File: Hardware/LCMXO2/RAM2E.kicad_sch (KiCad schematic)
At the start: 66 parts, among them J1 AppleIIeAux, J2 JTAG, J3 C14M, U1 LCMXO2-TG100, U2 W9812G6KH-6, U3 74LVC245APW, U4 74LVC245APW, U5 74LVC245APW, U6 74AHCT245PW, U7 74AHCT245PW, U8 XC6206P332MR, U9 AP2127K-1.2TRG1

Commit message: Change BOM to separate U4 from U3 and U5
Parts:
- U3, U5: value 74LVC245APW -> 74AHC245PW; LCSC Part C6082 -> C5516
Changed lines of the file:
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@@
       (effects (font (size 1.27 1.27)))
     )
-    (property "Value" "74LVC245APW" (at 76.2 53.34 0)
+    (property "Value" "74AHC245PW" (at 76.2 53.34 0)
       (effects (font (size 1.27 1.27)))
     )
@@
       (effects (font (size 1.524 1.524)) hide)
     )
-    (property "LCSC Part" "C6082" (at 76.2 38.1 0)
+    (property "LCSC Part" "C5516" (at 76.2 38.1 0)
       (effects (font (size 1.27 1.27)) hide)
     )
@@
       (effects (font (size 1.27 1.27)))
     )
-    (property "Value" "74LVC245APW" (at 76.2 119.38 0)
+    (property "Value" "74AHC245PW" (at 76.2 119.38 0)
       (effects (font (size 1.27 1.27)))
     )
@@
       (effects (font (size 1.524 1.524)) hide)
     )
-    (property "LCSC Part" "C6082" (at 76.2 104.14 0)
+    (property "LCSC Part" "C5516" (at 76.2 104.14 0)
       (effects (font (size 1.27 1.27)) hide)
     )

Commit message: RC 2.1
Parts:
- removed D1: Amber, stdpads:LED_0805, symbol Device:D_Small_ALT
- removed J2: JTAG, stdpads:TC2050, symbol Connector_Generic:Conn_02x05_Odd_Even
- removed J3: C14M, Connector_PinHeader_2.54mm:PinHeader_1x02_P2.54mm_Vertical, symbol Connector_Generic:Conn_01x02
- removed U9: AP2127K-1.2TRG1, stdpads:SOT-23-5, symbol Regulator_Linear:AP2127K-1.2
- added C32, C33: 22p, stdpads:C_0603, symbol Device:C_Small
- added C34, C36, C37: 2u2, stdpads:C_0603, symbol Device:C_Small
- added D1: Amber, stdpads:LED_0805, symbol Device:LED_Small_ALT
- added J2: microUSB, stdpads:USB_Micro-B_Amphenol_10118192-0001, symbol Connector:USB_B_Micro
- added J3: C14M, stdpads:EdgeClipHole, symbol Connector_Generic:Conn_01x01
- added J4: C14M, stdpads:PinHeader_1x02_P2.54mm_Vertical, symbol Connector_Generic:Conn_01x02
- added J5: JTAG, stdpads:Tag-Connect_TC2050-IDC-FP_2x05_P1.27mm_Vertical, symbol Connector_Generic:Conn_02x05_Odd_Even
- added R22: 47, stdpads:R_0603, symbol Device:R_Small
- added U10: CH340G, stdpads:SOIC-16_3.9mm, symbol Interface_USB:CH340G
- added U11: 74AHCT1G125GW, stdpads:SOT-353, symbol GW_Logic:741G125GW
- added U9: AP2127K-1.2TRG1, stdpads:SOT-23-5, symbol Regulator_Linear:AP2127K-1.8
- added Y1: 12M, stdpads:Crystal_SMD_3225-4Pin_3.2x2.5mm, symbol Device:Crystal_GND24_Small
- C1, C2, C3, C4, C5, C6: Mfg. Part Numbers Samsung CL21A106KAYNNNE -> (none); Notes 10V or higher. Any manufacturer's part is acceptable but Sa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 -> (none)
- C10, C11, C12, C13, C14, C15, C16, C17, C18, C19, C20, C21, C22, C23, C24, C25, C26, C27, C28, C30, C7, C8, C9: Mfg. Part Numbers Samsung CL10A225KO8NNNC -> (none); Notes 10V or higher. Any manufacturer's part is acceptable but Sa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 -> (none)
- C29: value 10u -> 2u2; footprint stdpads:C_0805 -> stdpads:C_0603; LCSC Part C15850 -> C23630; Mfg. Part Numbers Samsung CL21A106KAYNNNE -> (none); Notes 10V or higher. Any manufacturer's part is acceptable but Sa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 -> (none)
- C31: value 15p -> 22p; LCSC Part C1644 -> C1653; Mfg. Part Numbers Samsung CL10C150JB8NNNC -> (none); Notes 10V or higher. Any manufacturer's part is acceptable but Sa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 -> (none)
- FID1, FID2, FID3, FID4: Notes DNP - SMT vision system fiducial -> (none)
- H1, H2, H3, H4: Notes DNP - mounting hole for solder paste printing -> (none)
- H5: Notes DNP - mounting hole -> (none)
- J1: Notes DNP - edge connector -> (none)
- R1: Mfg. Part Numbers Uniroyal 0805W8F0000T5E -> (none); Notes Any manufacturer's part is acceptable. -> (none)
- R10: Mfg. Part Numbers Uniroyal 0805W8F2200T5E -> (none); Notes Any manufacturer's part is acceptable. -> (none)
- R11: Mfg. Part Numbers Uniroyal 0603WAF1002T5E -> (none); Notes Any manufacturer's part is acceptable. -> (none)
- R12, R13, R2, R3: Mfg. Part Numbers Uniroyal 0603WAF470JT5E -> (none); Notes Any manufacturer's part is acceptable. -> (none)
- R4: value 47 -> DNP; LCSC Part C23182 -> (none); Mfg. Part Numbers Uniroyal 0603WAF470JT5E -> (none); Notes Any manufacturer's part is acceptable. -> (none)
- R5, R8, R9: value 10k -> DNP; LCSC Part C25804 -> (none); Mfg. Part Numbers Uniroyal 0603WAF1002T5E -> (none); Notes Any manufacturer's part is acceptable. -> (none)
- R6: value 0 -> 2k2; footprint stdpads:R_0805 -> stdpads:R_0603; LCSC Part C17477 -> C4190; Mfg. Part Numbers Uniroyal 0805W8F0000T5E -> (none); Notes Any manufacturer's part is acceptable. -> (none)
- R7: footprint stdpads:R_0805 -> stdpads:R_0603
- U1: value LCMXO2-TG100 -> LCMXO2-640HC-4TG100C; Mfg. Part Numbers Lattice LCMXO2-640HC-4TG100C, Lattice LCMXO2-640HC-5TG100C,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 -> (none)
- U2: Mfg. Part Numbers Winbond W9812G6KH-6, Winbond W9812G6KH-6I, Winbond W9825G6K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 -> (none); Notes Most 166 MHz 128/256 Mbit x16 SDRAM is acceptable. -> (none)
- U3, U4, U5: Mfg. Part Numbers NXP 74LVC245APW, TI SN74LVC245APW, NXP 74AHC245PW, NXP 74AH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 -> (none); Notes Most 74LVC245 or 74AHC245 in TSSOP-20 package is acceptable. -> (none)
- U6, U7: Mfg. Part Numbers NXP 74AHCT245PW, NXP 74AHCT245APW, TI SN74AHCT245PW -> (none); Notes Most 74AHCT245 in TSSOP-20 package is acceptable. -> (none)
- U8: Mfg. Part Numbers Torex XC6206P332MR -> (none); Notes Most 3.3V regulator in SOT-23 package is acceptable. -> (none)
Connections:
- net +1V2: now also U9.5 (VOUT)
- net +3V3: now also R6.1, R9.1, C34.1, C36.1, J5.6 (Pin_6), U10.10 (~{DSR}), U10.11 (~{RI}), U10.16 (VCC), U10.3 (RXD), U10.4 (V3); no longer C30.1
- net +5V: now also C30.1, U11.5 (Vcc), U9.1 (VIN), U9.3 (EN)
- net ACLK: now also R12.1; no longer R13.1
- net AN3: now also U11.2 (A); no longer R6.2, R7.2
- net C14MB: now also R13.1, J3.1 (Pin_1), J4.1 (Pin_1); no longer R3.1
- net GND: now also R7.2, C32.2, C33.2, C34.2, C36.2, C37.2, J2.5 (GND), J2.6 (Shield), J4.2 (Pin_2), J5.2 (Pin_2), J5.4 (Pin_4), U10.1 (GND), U10.12 (~{DCD}), U10.15 (R232), U11.3 (GND), U9.2 (GND), Y1.2, Y1.4; no longer R9.2
- net LED: now also D1.1 (K)
- net RCLK: now also R3.1; no longer R12.1
- net R~{W}: now also U3.3 (A1); no longer U3.2 (A0)
- net R~{W}in: now also U3.17 (B1); no longer U3.18 (B0)
- net TCK: now also C31.1, R4.1, R7.1, U1.91 (TCK/PT7C), R22.2; no longer R4.2
- net TCKr: now also R4.2, J5.1 (Pin_1); no longer C31.1, R4.1, R9.1, U1.91 (TCK/PT7C)
- net TDI: now also J5.5 (Pin_5), U10.13 (~{DTR})
- net TDO: now also J5.7 (Pin_7), U10.9 (~{CTS})
- net TMS: now also R9.2, J5.3 (Pin_3), U10.14 (~{RTS})
- net ~{C07X}: now also U3.2 (A0); no longer U3.3 (A1)
- net ~{C07X}in: now also U3.18 (B0); no longer U3.17 (B1)
- net ~{FRCTXT}: now also U11.4 (Y); no longer R6.1, R7.1
- net at R12.2, U4.16 (B2): now also R3.2; no longer R13.2
- net at U4.18 (B0): now also R13.2; no longer R3.2
- net DHGR~{OE}: now reaches U1.47 (PB14)
- net DHGR~{OE}: now also R6.2, U11.1 (~{OE})
- net at R10.1: now also D1.2 (A)
- new net: C33.1, U10.7 (XI), Y1.1
- new net: C32.1, U10.8 (XO), Y1.3
- new net: J2.2 (D-), U10.6 (UD-)
- new net: J2.3 (D+), U10.5 (UD+)
- new net USB5V: C37.1, J2.1 (VBUS)
- new net UTCK: R22.1, U10.2 (TXD)
- no-connect marks 4 -> 5
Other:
- moved on the sheet: R11, R5, R8

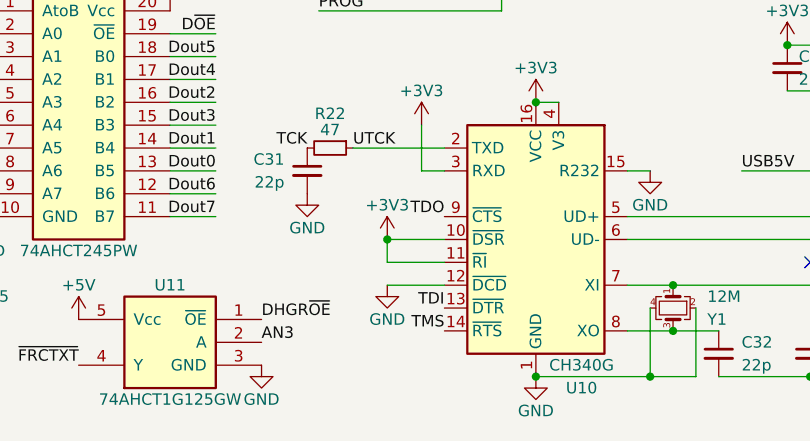
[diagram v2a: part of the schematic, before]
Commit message: RC
Fix board IDs
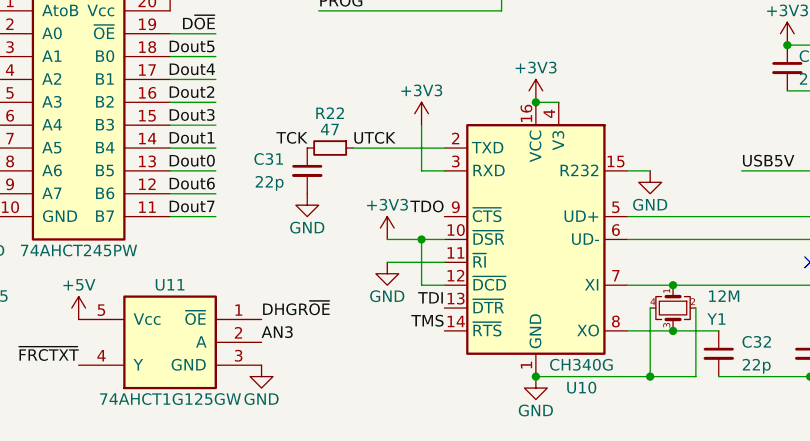
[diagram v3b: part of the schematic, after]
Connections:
- net +3V3: now also U10.12 (~{DCD}); no longer U10.11 (~{RI})
- net GND: now also U10.11 (~{RI}); no longer U10.12 (~{DCD})
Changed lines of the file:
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@@
   (junction (at 168.91 165.1) (diameter 0) (color 0 0 0 0)
   )
+  (junction (at 99.06 181.61) (diameter 0) (color 0 0 0 0)
+  )
   (junction (at 208.28 80.01) (diameter 0) (color 0 0 0 0)
   )
@@
   )
   (junction (at 199.39 19.05) (diameter 0) (color 0 0 0 0)
-  )
-  (junction (at 95.25 181.61) (diameter 0) (color 0 0 0 0)
   )
   (junction (at 198.12 85.09) (diameter 0) (color 0 0 0 0)
@@
     (stroke (width 0) (type default))
   )
-  (wire (pts (xy 95.25 186.69) (xy 101.6 186.69))
-    (stroke (width 0) (type default))
-  )
   (wire (pts (xy 38.1 83.82) (xy 34.29 83.82))
     (stroke (width 0) (type default))
   )
+  (wire (pts (xy 101.6 186.69) (xy 99.06 186.69))
+    (stroke (width 0) (type default))
+  )
   (wire (pts (xy 129.54 196.85) (xy 124.46 196.85))
     (stroke (width 0) (type default))
@@
     (stroke (width 0) (type default))
   )
+  (wire (pts (xy 99.06 186.69) (xy 99.06 181.61))
+    (stroke (width 0) (type default))
+  )
   (wire (pts (xy 45.72 102.87) (xy 50.8 102.87))
     (stroke (width 0) (type default))
@@
     (stroke (width 0) (type default))
   )
+  (wire (pts (xy 99.06 181.61) (xy 101.6 181.61))
+    (stroke (width 0) (type default))
+  )
   (wire (pts (xy 114.3 44.45) (xy 119.38 44.45))
     (stroke (width 0) (type default))
@@
     (stroke (width 0) (type default))
   )
-  (wire (pts (xy 95.25 181.61) (xy 101.6 181.61))
+  (wire (pts (xy 95.25 181.61) (xy 99.06 181.61))
     (stroke (width 0) (type default))
   )
@@
   )
   (wire (pts (xy 199.39 19.05) (xy 199.39 21.59))
-    (stroke (width 0) (type default))
-  )
-  (wire (pts (xy 95.25 184.15) (xy 95.25 181.61))
     (stroke (width 0) (type default))
   )
@@
     )
   )
-  (symbol (lib_id "power:GND") (at 95.25 186.69 0) (mirror y) (unit 1)
+  (symbol (lib_id "power:GND") (at 95.25 184.15 0) (mirror y) (unit 1)
     (in_bom yes) (on_board yes) (dnp no)
-    (property "Reference" "#PWR033" (at 95.25 193.04 0)
-      (effects (font (size 1.27 1.27)) hide)
-    )
-    (property "Value" "GND" (at 95.25 190.5 0)
+    (property "Reference" "#PWR033" (at 95.25 190.5 0)
+      (effects (font (size 1.27 1.27)) hide)
+    )
+    (property "Value" "GND" (at 95.25 187.96 0)
       (effects (font (size 1.27 1.27)))
     )
-    (property "Footprint" "" (at 95.25 186.69 0)
-      (effects (font (size 1.27 1.27)) hide)
-    )
-    (property "Datasheet" "" (at 95.25 186.69 0)
-      (effects (font (size 1.27 1.27)) hide)
-    )
+    (property "Footprint" "" (at 95.25 184.15 0)
+      (effects (font (size 1.27 1.27)) hide)
+    )
+    (property "Datasheet" "" (at 95.25 184.15 0)
+      (effects (font (size 1.27 1.27)) hide)
+    )

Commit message: RC
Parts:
- added R14, R15: 2k2, stdpads:R_0603, symbol Device:R_Small
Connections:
- net +3V3: now also R14.1, R15.1
- net D~{OE}: now also R15.2
- net V~{OE}: now also R14.2
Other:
- moved on the sheet: R11, R5, R8

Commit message: RC
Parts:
- U3, U5: value 74AHC245PW -> 74LVC245APW; LCSC Part C5516 -> C6082
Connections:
- no-connect marks 5 -> 6
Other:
- title: GW4203B (RAM2E II) - LCMXO2-640 / LCMXO2-1200 -> GW4203C (RAM2E II) - LCMXO2-640 / LCMXO2-1200
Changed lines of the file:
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@@
   (paper "USLetter")
   (title_block
-    (title "GW4203B (RAM2E II) - LCMXO2-640 / LCMXO2-1200")
-    (date "2024-04-24")
-    (rev "2.1")
+    (title "GW4203C (RAM2E II) - LCMXO2-640 / LCMXO2-1200")
+    (date "2024-05-20")
+    (rev "1.0")
     (company "Garrett's Workshop")
   )
@@
   (no_connect (at 71.12 64.77))
   (no_connect (at 142.24 184.15))
+  (no_connect (at 119.38 125.73))
   (no_connect (at 21.59 88.9))
   (bus_entry (at 210.82 107.95) (size -2.54 2.54)
@@
       (effects (font (size 1.27 1.27)))
     )
-    (property "Value" "74AHC245PW" (at 60.96 50.8 0)
+    (property "Value" "74LVC245APW" (at 60.96 50.8 0)
       (effects (font (size 1.27 1.27)))
     )
@@
       (effects (font (size 1.524 1.524)) hide)
     )
-    (property "LCSC Part" "C5516" (at 60.96 35.56 0)
+    (property "LCSC Part" "C6082" (at 60.96 35.56 0)
       (effects (font (size 1.27 1.27)) hide)
     )
@@
       (effects (font (size 1.27 1.27)))
     )
-    (property "Value" "74AHC245PW" (at 60.96 116.84 0)
+    (property "Value" "74LVC245APW" (at 60.96 116.84 0)
       (effects (font (size 1.27 1.27)))
     )
@@
       (effects (font (size 1.524 1.524)) hide)
     )
-    (property "LCSC Part" "C5516" (at 60.96 101.6 0)
+    (property "LCSC Part" "C6082" (at 60.96 101.6 0)
       (effects (font (size 1.27 1.27)) hide)
     )

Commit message: RC
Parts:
- C29: value 2u2 -> 10u; footprint stdpads:C_0603 -> stdpads:C_0805; LCSC Part C23630 -> C15850
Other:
- moved on the sheet: C30
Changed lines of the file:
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@@
   (junction (at 218.44 54.61) (diameter 0) (color 0 0 0 0)
   )
+  (junction (at 208.28 85.09) (diameter 0) (color 0 0 0 0)
+  )
   (junction (at 218.44 69.85) (diameter 0) (color 0 0 0 0)
   )
@@
   (junction (at 99.06 181.61) (diameter 0) (color 0 0 0 0)
   )
-  (junction (at 208.28 80.01) (diameter 0) (color 0 0 0 0)
-  )
   (junction (at 228.6 74.93) (diameter 0) (color 0 0 0 0)
   )
@@
   (junction (at 228.6 44.45) (diameter 0) (color 0 0 0 0)
   )
-  (junction (at 218.44 85.09) (diameter 0) (color 0 0 0 0)
-  )
   (junction (at 187.96 19.05) (diameter 0) (color 0 0 0 0)
   )
@@
   (junction (at 187.96 80.01) (diameter 0) (color 0 0 0 0)
   )
+  (junction (at 218.44 85.09) (diameter 0) (color 0 0 0 0)
+  )
   (junction (at 238.76 85.09) (diameter 0) (color 0 0 0 0)
   )
@@
   (junction (at 17.78 36.83) (diameter 0) (color 0 0 0 0)
   )
+  (junction (at 208.28 80.01) (diameter 0) (color 0 0 0 0)
+  )
   (junction (at 238.76 54.61) (diameter 0) (color 0 0 0 0)
   )
@@
   (junction (at 218.44 74.93) (diameter 0) (color 0 0 0 0)
   )
-  (junction (at 208.28 85.09) (diameter 0) (color 0 0 0 0)
-  )
   (junction (at 198.12 74.93) (diameter 0) (color 0 0 0 0)
   )
@@
     (stroke (width 0) (type default))
   )
+  (wire (pts (xy 208.28 85.09) (xy 218.44 85.09))
+    (stroke (width 0) (type default))
+  )
   (wire (pts (xy 114.3 87.63) (xy 119.38 87.63))
     (stroke (width 0) (type default))
@@
     (stroke (width 0) (type default))
   )
-  (wire (pts (xy 218.44 85.09) (xy 228.6 85.09))
-    (stroke (width 0) (type default))
-  )
   (wire (pts (xy 114.3 69.85) (xy 119.38 69.85))
     (stroke (width 0) (type default))
@@
     (stroke (width 0) (type default))
   )
+  (wire (pts (xy 208.28 80.01) (xy 218.44 80.01))
+    (stroke (width 0) (type default))
+  )
   (wire (pts (xy 138.43 21.59) (xy 140.97 21.59))
     (stroke (width 0) (type default))
@@
     (stroke (width 0) (type default))
   )
-  (wire (pts (xy 208.28 85.09) (xy 218.44 85.09))
-    (stroke (width 0) (type default))
-  )
   (wire (pts (xy 45.72 31.75) (xy 50.8 31.75))
     (stroke (width 0) (type default))
@@
     (stroke (width 0) (type default))
   )
+  (wire (pts (xy 218.44 85.09) (xy 228.6 85.09))
+    (stroke (width 0) (type default))
+  )
   (wire (pts (xy 218.44 44.45) (xy 218.44 41.91))
     (stroke (width 0) (type default))
@@
     (stroke (width 0) (type default))
   )
-  (wire (pts (xy 208.28 80.01) (xy 218.44 80.01))
-    (stroke (width 0) (type default))
-  )
   (wire (pts (xy 76.2 161.29) (xy 71.12 161.29))
     (stroke (width 0) (type default))
@@
     )
   )
-  (symbol (lib_id "Device:C_Small") (at 218.44 82.55 0) (unit 1)
+  (symbol (lib_id "Device:C_Small") (at 208.28 82.55 0) (unit 1)
     (in_bom yes) (on_board yes) (dnp no)
-    (property "Reference" "C30" (at 219.71 81.28 0)
+    (property "Reference" "C30" (at 209.55 81.28 0)
       (effects (font (size 1.27 1.27)) (justify left))
     )
-    (property "Value" "2u2" (at 219.71 83.82 0)
+    (property "Value" "2u2" (at 209.55 83.82 0)
       (effects (font (size 1.27 1.27)) (justify left))
     )
-    (property "Footprint" "stdpads:C_0603" (at 218.44 82.55 0)
+    (property "Footprint" "stdpads:C_0603" (at 208.28 82.55 0)
       (effects (font (size 1.27 1.27)) hide)
     )
-    (property "Datasheet" "" (at 218.44 82.55 0)
+    (property "Datasheet" "" (at 208.28 82.55 0)
       (effects (font (size 1.27 1.27)) hide)
     )
-    (property "LCSC Part" "C23630" (at 218.44 82.55 0)
+    (property "LCSC Part" "C23630" (at 208.28 82.55 0)
       (effects (font (size 1.27 1.27)) hide)
     )
@@
     )
   )
+  (symbol (lib_id "Device:C_Small") (at 218.44 82.55 0) (unit 1)
+    (in_bom yes) (on_board yes) (dnp no)
+    (property "Reference" "C29" (at 219.71 81.28 0)
+      (effects (font (size 1.27 1.27)) (justify left))
+    )
+    (property "Value" "10u" (at 219.71 83.82 0)
+      (effects (font (size 1.27 1.27)) (justify left))
+    )
+    (property "Footprint" "stdpads:C_0805" (at 218.44 82.55 0)
+      (effects (font (size 1.27 1.27)) hide)
+    )
+    (property "Datasheet" "" (at 218.44 82.55 0)
+      (effects (font (size 1.27 1.27)) hide)
+    )
+    (property "LCSC Part" "C15850" (at 218.44 82.55 0)
+      (effects (font (size 1.27 1.27)) hide)
+    )
+    (pin "1")
+    (pin "2")
+    (instances
+      (project "RAM2E"
+        (path "/805baf6f-a2ba-4145-8b5a-40874bf6761b"
+          (reference "C29") (unit 1)
+        )
+      )
+    )
+  )
   (symbol (lib_id "power:GND") (at 45.72 151.13 0) (mirror y) (unit 1)
     (in_bom yes) (on_board yes) (dnp no)
@@
         )
       )
-    )
-  )
-  (symbol (lib_id "Device:C_Small") (at 208.28 82.55 0) (unit 1)
-    (in_bom yes) (on_board yes) (dnp no)
-    (property "Reference" "C29" (at 209.55 81.28 0)
-      (effects (font (size 1.27 1.27)) (justify left))
-    )
-    (property "Value" "2u2" (at 209.55 83.82 0)
-      (effects (font (size 1.27 1.27)) (justify left))
-    )
-    (property "Footprint" "stdpads:C_0603" (at 208.28 82.55 0)
-      (effects (font (size 1.27 1.27)) hide)
-    )
-    (property "Datasheet" "" (at 208.28 82.55 0)
-      (effects (font (size 1.27 1.27)) hide)
-    )
-    (property "LCSC Part" "C23630" (at 208.28 82.55 0)
-      (effects (font (size 1.27 1.27)) hide)
-    )
-    (pin "1")
-    (pin "2")
-    (instances
-      (project "RAM2E"
-        (path "/805baf6f-a2ba-4145-8b5a-40874bf6761b"
-          (reference "C29") (unit 1)
-        )
-      )

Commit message: RC C.1.1
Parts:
- H1, H2, H3, H4, H5: value (none) -> (none)
- R1: value 0 -> 0
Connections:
- net +3V3: now also U1.11 ((VccIO3))
- no-connect marks 6 -> 8
